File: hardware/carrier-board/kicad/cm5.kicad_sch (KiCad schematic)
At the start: 6 parts, among them J30 FAN, J31 FAN, Q10 NMOS, Q11 NMOS, U2 CM5

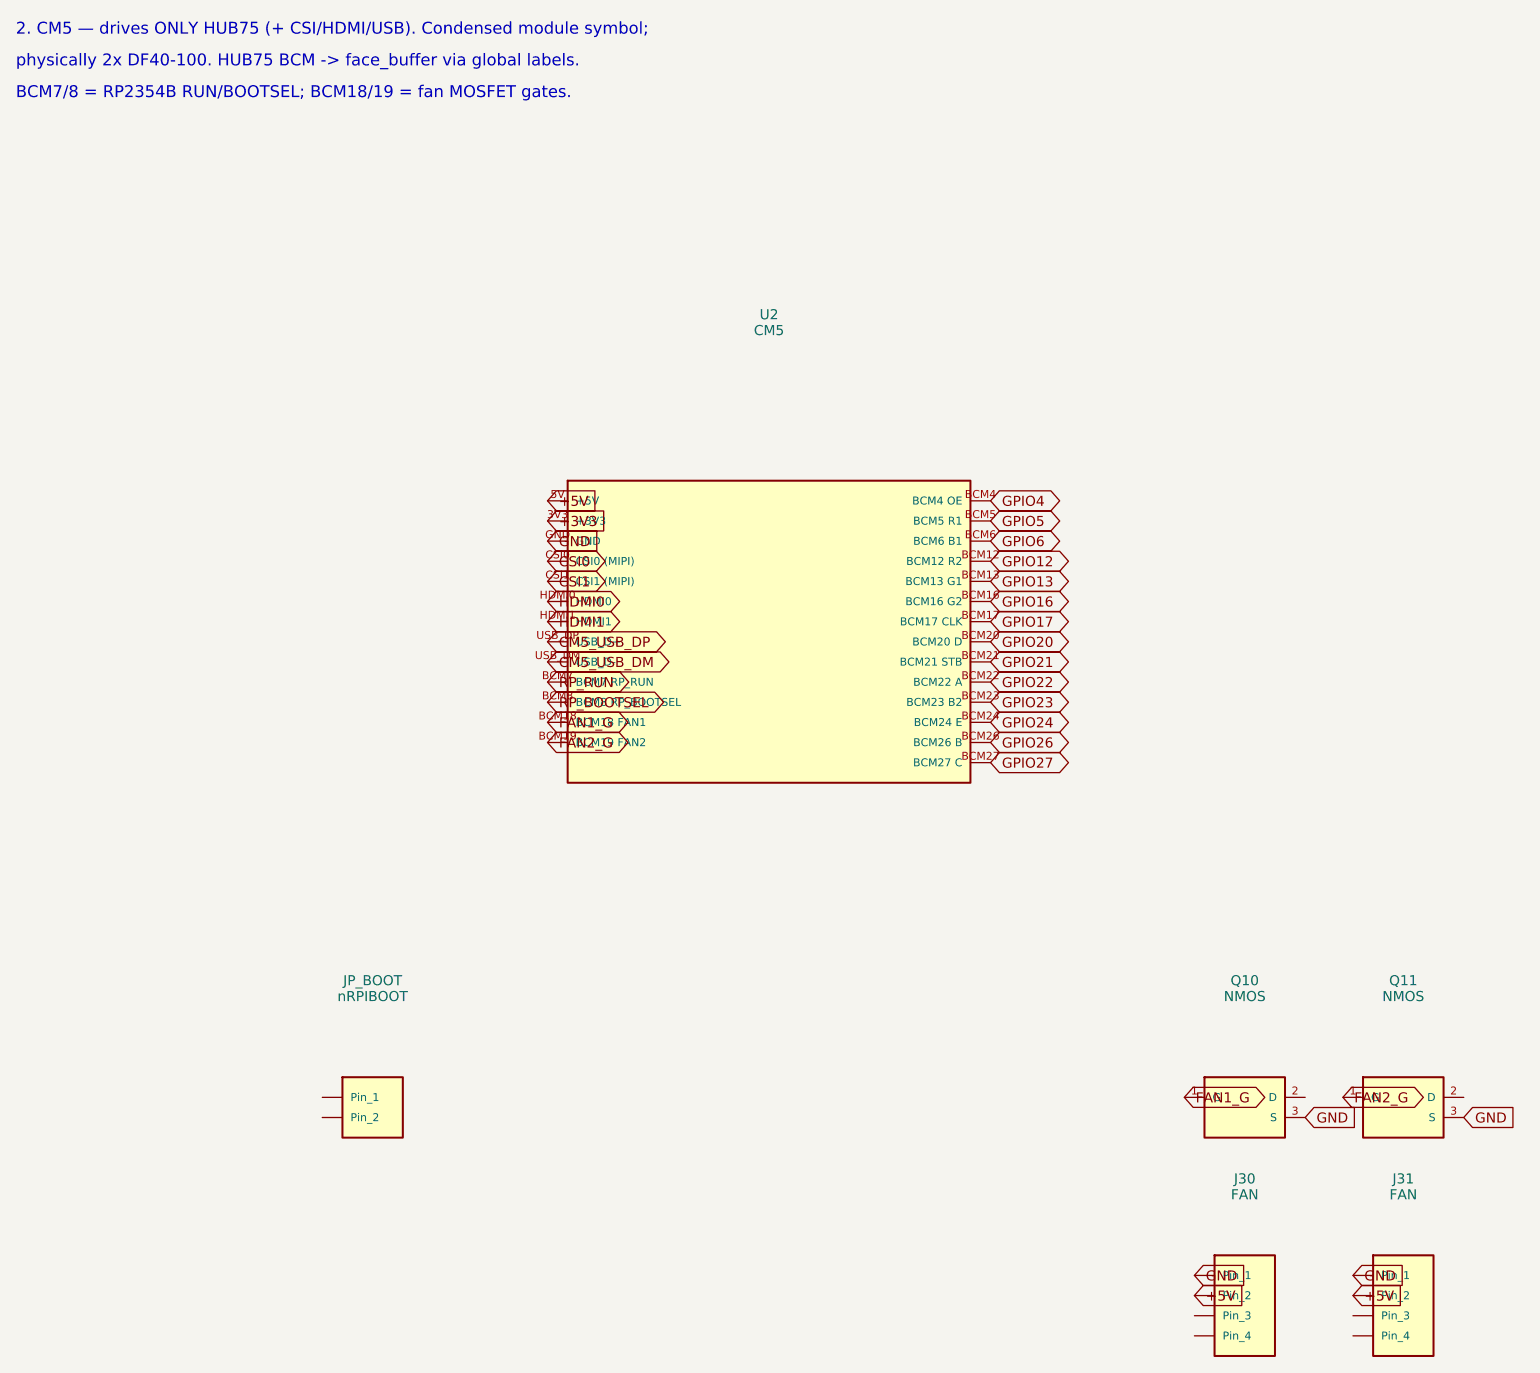
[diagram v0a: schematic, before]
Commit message: hardware(carrier): replace USB 2.0 hub with VL817 USB 3.1 4-port hub
Swap the on-board USB2514B (USB 2.0) for a VIA VL817 4-port USB 3.1 Gen1
(5 Gbps) hub with four USB-C downstream receptacles (J40-J43), upstream on
a CM5 USB 3.0 port. The CM5 exposes 2x USB 3.0 + 1x USB 2.0, so:

  - USB3 #0 -> VL817 upstream (SuperSpeed + USB 2.0)
  - USB3 #1 -> RP2354B CDC (now OFF-hub, via SW1) -> frees all 4 hub ports
  - USB2    -> backpack phone uplink (J11)

Generator (populate_sheets.py):
  - new VL817 condensed symbol (USB2 + SS per port, xtal, reset, straps)
  - new USB-C 3.1 receptacle symbol (VBUS/GND/CC/D+-/one SS lane)
  - CM5 symbol gains USB3 SuperSpeed pins + 2nd/3rd USB ports
  - rewrite sh_usb(): per-port CC Rp pull-ups (56k, host/DFP), VBUS PTC off
    +5V, USBLC6 ESD, SS AC-coupling caps at each TX, 25 MHz hub clock
  - SW1 'A' side rerouted from hub to the dedicated CM5 USB port

Docs: CONNECTORS, POWER, BOM, REQUIREMENTS, BLOCK-DIAGRAM, READMEs updated
for the USB 3.1 hub, USB-C downstream ports, and off-hub RP2354B link.

All 11 sheets regenerated; S-expressions balanced and cross-sheet global
nets verified consistent.

Co-Authored-By: Claude Opus 4.8 <noreply@anthropic.com>
Claude-Session: https://claude.ai/code/session_01DgiE5SHRCeyk1gvfvshMGa
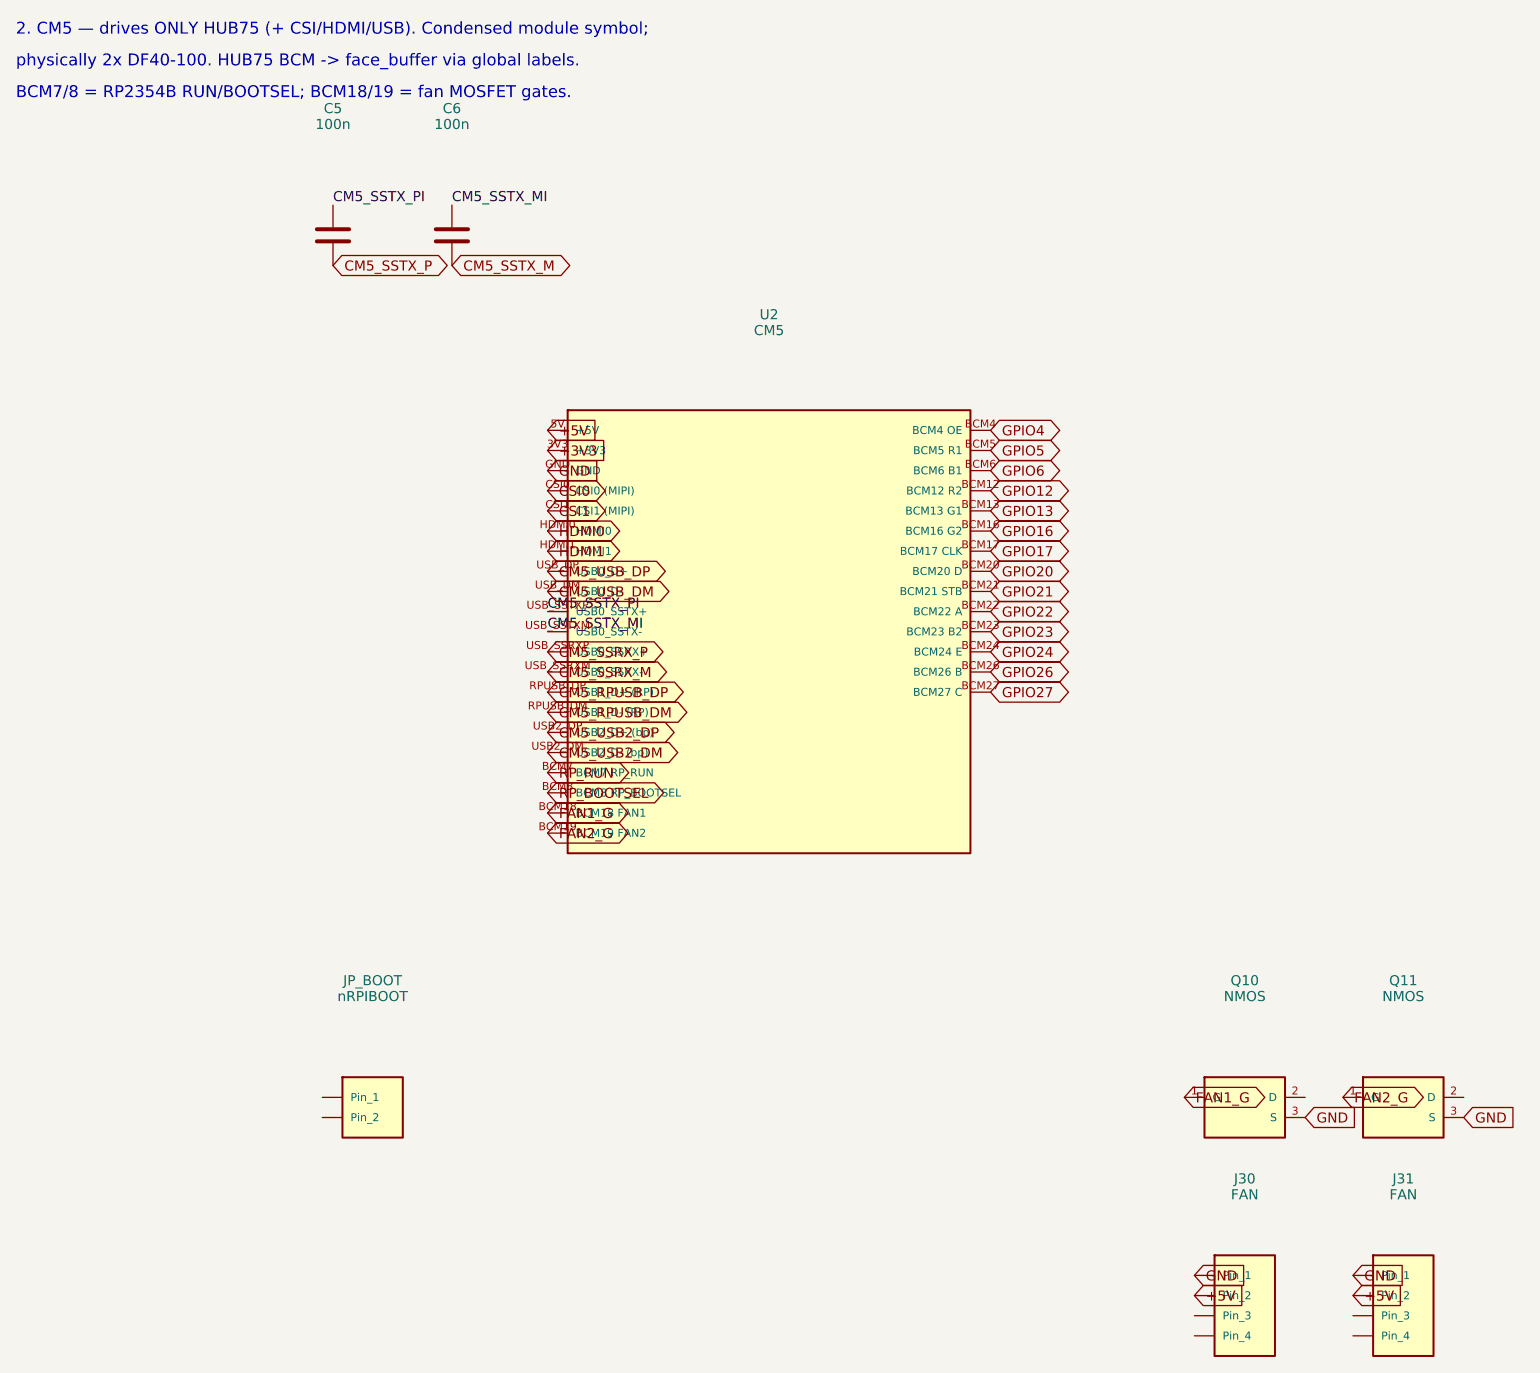
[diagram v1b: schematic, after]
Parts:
- added C5, C6: 100n, symbol Device:C
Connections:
- new net CM5_RPUSB_DM: U2.RPUSB_DM (USB1_D- (RP))
- new net CM5_RPUSB_DP: U2.RPUSB_DP (USB1_D+ (RP))
- new net CM5_SSRX_M: U2.USB_SSRXM (USB0_SSRX-)
- new net CM5_SSRX_P: U2.USB_SSRXP (USB0_SSRX+)
- new net CM5_SSTX_M: C6.2
- new net CM5_SSTX_MI: C6.1, U2.USB_SSTXM (USB0_SSTX-)
- new net CM5_SSTX_P: C5.2
- new net CM5_SSTX_PI: C5.1, U2.USB_SSTXP (USB0_SSTX+)
- new net CM5_USB2_DM: U2.USB2_DM (USB2_D- (bp))
- new net CM5_USB2_DP: U2.USB2_DP (USB2_D+ (bp))
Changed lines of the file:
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@@
     (pin "USB_DP")
     (pin "USB_DM")
+    (pin "USB_SSTXP")
+    (pin "USB_SSTXM")
+    (pin "USB_SSRXP")
+    (pin "USB_SSRXM")
+    (pin "RPUSB_DP")
+    (pin "RPUSB_DM")
+    (pin "USB2_DP")
+    (pin "USB2_DM")
     (pin "BCM7")
     (pin "BCM8")
@@
         (path "/3812e784-9e95-4c5b-856a-ca4e97dc1851"
           (reference "U2") (unit 1))))
+  )
+  (symbol
+    (lib_id "Device:C")
+    (at 55.00 40.00 0)
+    (unit 1)
+    (exclude_from_sim no) (in_bom yes) (on_board yes) (dnp no)
+    (property "Reference" "C5" (at 55.00 24.00 0) (effects (font (size 1.27 1.27))))
+    (property "Value" "100n" (at 55.00 26.00 0) (effects (font (size 1.27 1.27))))
+    (property "Footprint" "" (at 55.00 40.00 0) (effects (font (size 1.27 1.27)) (hide yes)))
+    (property "Datasheet" "" (at 55.00 40.00 0) (effects (font (size 1.27 1.27)) (hide yes)))
+    (pin "1")
+    (pin "2")
+    (instances
+      (project "ProtoHUD-Carrier"
+        (path "/3812e784-9e95-4c5b-856a-ca4e97dc1851"
+          (reference "C5") (unit 1))))
+  )
+  (symbol
+    (lib_id "Device:C")
+    (at 70.00 40.00 0)
+    (unit 1)
+    (exclude_from_sim no) (in_bom yes) (on_board yes) (dnp no)
+    (property "Reference" "C6" (at 70.00 24.00 0) (effects (font (size 1.27 1.27))))
+    (property "Value" "100n" (at 70.00 26.00 0) (effects (font (size 1.27 1.27))))
+    (property "Footprint" "" (at 70.00 40.00 0) (effects (font (size 1.27 1.27)) (hide yes)))
+    (property "Datasheet" "" (at 70.00 40.00 0) (effects (font (size 1.27 1.27)) (hide yes)))
+    (pin "1")
+    (pin "2")
+    (instances
+      (project "ProtoHUD-Carrier"
+        (path "/3812e784-9e95-4c5b-856a-ca4e97dc1851"
+          (reference "C6") (unit 1))))
   )
   (symbol
@@
           (reference "JP_BOOT") (unit 1))))
   )
-  (global_label "+5V" (shape input) (at 82.06 73.49 180) (effects (font (size 1.27 1.27)) (justify left)))
-  (global_label "+3V3" (shape input) (at 82.06 76.03 180) (effects (font (size 1.27 1.27)) (justify left)))
-  (global_label "GND" (shape input) (at 82.06 78.57 180) (effects (font (size 1.27 1.27)) (justify left)))
-  (global_label "CSI0" (shape bidirectional) (at 82.06 81.11 180) (effects (font (size 1.27 1.27)) (justify left)))
-  (global_label "CSI1" (shape bidirectional) (at 82.06 83.65 180) (effects (font (size 1.27 1.27)) (justify left)))
-  (global_label "HDMI0" (shape bidirectional) (at 82.06 86.19 180) (effects (font (size 1.27 1.27)) (justify left)))
-  (global_label "HDMI1" (shape bidirectional) (at 82.06 88.73 180) (effects (font (size 1.27 1.27)) (justify left)))
-  (global_label "CM5_USB_DP" (shape bidirectional) (at 82.06 91.27 180) (effects (font (size 1.27 1.27)) (justify left)))
-  (global_label "CM5_USB_DM" (shape bidirectional) (at 82.06 93.81 180) (effects (font (size 1.27 1.27)) (justify left)))
-  (global_label "RP_RUN" (shape bidirectional) (at 82.06 96.35 180) (effects (font (size 1.27 1.27)) (justify left)))
-  (global_label "RP_BOOTSEL" (shape bidirectional) (at 82.06 98.89 180) (effects (font (size 1.27 1.27)) (justify left)))
-  (global_label "FAN1_G" (shape bidirectional) (at 82.06 101.43 180) (effects (font (size 1.27 1.27)) (justify left)))
-  (global_label "FAN2_G" (shape bidirectional) (at 82.06 103.97 180) (effects (font (size 1.27 1.27)) (justify left)))
-  (global_label "GPIO4" (shape bidirectional) (at 137.94 73.49 0) (effects (font (size 1.27 1.27)) (justify left)))
-  (global_label "GPIO5" (shape bidirectional) (at 137.94 76.03 0) (effects (font (size 1.27 1.27)) (justify left)))
-  (global_label "GPIO6" (shape bidirectional) (at 137.94 78.57 0) (effects (font (size 1.27 1.27)) (justify left)))
-  (global_label "GPIO12" (shape bidirectional) (at 137.94 81.11 0) (effects (font (size 1.27 1.27)) (justify left)))
-  (global_label "GPIO13" (shape bidirectional) (at 137.94 83.65 0) (effects (font (size 1.27 1.27)) (justify left)))
-  (global_label "GPIO16" (shape bidirectional) (at 137.94 86.19 0) (effects (font (size 1.27 1.27)) (justify left)))
-  (global_label "GPIO17" (shape bidirectional) (at 137.94 88.73 0) (effects (font (size 1.27 1.27)) (justify left)))
-  (global_label "GPIO20" (shape bidirectional) (at 137.94 91.27 0) (effects (font (size 1.27 1.27)) (justify left)))
-  (global_label "GPIO21" (shape bidirectional) (at 137.94 93.81 0) (effects (font (size 1.27 1.27)) (justify left)))
-  (global_label "GPIO22" (shape bidirectional) (at 137.94 96.35 0) (effects (font (size 1.27 1.27)) (justify left)))
-  (global_label "GPIO23" (shape bidirectional) (at 137.94 98.89 0) (effects (font (size 1.27 1.27)) (justify left)))
-  (global_label "GPIO24" (shape bidirectional) (at 137.94 101.43 0) (effects (font (size 1.27 1.27)) (justify left)))
-  (global_label "GPIO26" (shape bidirectional) (at 137.94 103.97 0) (effects (font (size 1.27 1.27)) (justify left)))
-  (global_label "GPIO27" (shape bidirectional) (at 137.94 106.51 0) (effects (font (size 1.27 1.27)) (justify left)))
+  (global_label "+5V" (shape input) (at 82.06 64.60 180) (effects (font (size 1.27 1.27)) (justify left)))
+  (global_label "+3V3" (shape input) (at 82.06 67.14 180) (effects (font (size 1.27 1.27)) (justify left)))
+  (global_label "GND" (shape input) (at 82.06 69.68 180) (effects (font (size 1.27 1.27)) (justify left)))
+  (global_label "CSI0" (shape bidirectional) (at 82.06 72.22 180) (effects (font (size 1.27 1.27)) (justify left)))
+  (global_label "CSI1" (shape bidirectional) (at 82.06 74.76 180) (effects (font (size 1.27 1.27)) (justify left)))
+  (global_label "HDMI0" (shape bidirectional) (at 82.06 77.30 180) (effects (font (size 1.27 1.27)) (justify left)))
+  (global_label "HDMI1" (shape bidirectional) (at 82.06 79.84 180) (effects (font (size 1.27 1.27)) (justify left)))
+  (global_label "CM5_USB_DP" (shape bidirectional) (at 82.06 82.38 180) (effects (font (size 1.27 1.27)) (justify left)))
+  (global_label "CM5_USB_DM" (shape bidirectional) (at 82.06 84.92 180) (effects (font (size 1.27 1.27)) (justify left)))
+  (global_label "CM5_SSRX_P" (shape bidirectional) (at 82.06 92.54 180) (effects (font (size 1.27 1.27)) (justify left)))
+  (global_label "CM5_SSRX_M" (shape bidirectional) (at 82.06 95.08 180) (effects (font (size 1.27 1.27)) (justify left)))
+  (global_label "CM5_RPUSB_DP" (shape bidirectional) (at 82.06 97.62 180) (effects (font (size 1.27 1.27)) (justify left)))
+  (global_label "CM5_RPUSB_DM" (shape bidirectional) (at 82.06 100.16 180) (effects (font (size 1.27 1.27)) (justify left)))
+  (global_label "CM5_USB2_DP" (shape bidirectional) (at 82.06 102.70 180) (effects (font (size 1.27 1.27)) (justify left)))
+  (global_label "CM5_USB2_DM" (shape bidirectional) (at 82.06 105.24 180) (effects (font (size 1.27 1.27)) (justify left)))
+  (global_label "RP_RUN" (shape bidirectional) (at 82.06 107.78 180) (effects (font (size 1.27 1.27)) (justify left)))
+  (global_label "RP_BOOTSEL" (shape bidirectional) (at 82.06 110.32 180) (effects (font (size 1.27 1.27)) (justify left)))
+  (global_label "FAN1_G" (shape bidirectional) (at 82.06 112.86 180) (effects (font (size 1.27 1.27)) (justify left)))
+  (global_label "FAN2_G" (shape bidirectional) (at 82.06 115.40 180) (effects (font (size 1.27 1.27)) (justify left)))
+  (label "CM5_SSTX_PI" (at 55.00 36.19 0) (effects (font (size 1.27 1.27)) (justify left bottom)))
+  (global_label "CM5_SSTX_P" (shape bidirectional) (at 55.00 43.81 0) (effects (font (size 1.27 1.27)) (justify left)))
+  (label "CM5_SSTX_MI" (at 70.00 36.19 0) (effects (font (size 1.27 1.27)) (justify left bottom)))
+  (global_label "CM5_SSTX_M" (shape bidirectional) (at 70.00 43.81 0) (effects (font (size 1.27 1.27)) (justify left)))
+  (label "CM5_SSTX_PI" (at 82.06 87.46 180) (effects (font (size 1.27 1.27)) (justify left bottom)))
+  (label "CM5_SSTX_MI" (at 82.06 90.00 180) (effects (font (size 1.27 1.27)) (justify left bottom)))
+  (global_label "GPIO4" (shape bidirectional) (at 137.94 64.60 0) (effects (font (size 1.27 1.27)) (justify left)))
+  (global_label "GPIO5" (shape bidirectional) (at 137.94 67.14 0) (effects (font (size 1.27 1.27)) (justify left)))
+  (global_label "GPIO6" (shape bidirectional) (at 137.94 69.68 0) (effects (font (size 1.27 1.27)) (justify left)))
+  (global_label "GPIO12" (shape bidirectional) (at 137.94 72.22 0) (effects (font (size 1.27 1.27)) (justify left)))
+  (global_label "GPIO13" (shape bidirectional) (at 137.94 74.76 0) (effects (font (size 1.27 1.27)) (justify left)))
+  (global_label "GPIO16" (shape bidirectional) (at 137.94 77.30 0) (effects (font (size 1.27 1.27)) (justify left)))
+  (global_label "GPIO17" (shape bidirectional) (at 137.94 79.84 0) (effects (font (size 1.27 1.27)) (justify left)))
+  (global_label "GPIO20" (shape bidirectional) (at 137.94 82.38 0) (effects (font (size 1.27 1.27)) (justify left)))
+  (global_label "GPIO21" (shape bidirectional) (at 137.94 84.92 0) (effects (font (size 1.27 1.27)) (justify left)))
+  (global_label "GPIO22" (shape bidirectional) (at 137.94 87.46 0) (effects (font (size 1.27 1.27)) (justify left)))
+  (global_label "GPIO23" (shape bidirectional) (at 137.94 90.00 0) (effects (font (size 1.27 1.27)) (justify left)))
+  (global_label "GPIO24" (shape bidirectional) (at 137.94 92.54 0) (effects (font (size 1.27 1.27)) (justify left)))
+  (global_label "GPIO26" (shape bidirectional) (at 137.94 95.08 0) (effects (font (size 1.27 1.27)) (justify left)))
+  (global_label "GPIO27" (shape bidirectional) (at 137.94 97.62 0) (effects (font (size 1.27 1.27)) (justify left)))
   (global_label "FAN1_G" (shape bidirectional) (at 162.38 148.73 180) (effects (font (size 1.27 1.27)) (justify left)))
   (global_label "GND" (shape input) (at 177.62 151.27 0) (effects (font (size 1.27 1.27)) (justify left)))
